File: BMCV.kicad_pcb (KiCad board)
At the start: 4 copper layers, 80 x 108 mm, 363 parts, among them J1 AudioJack2_SwitchT, J10 AudioJack2_SwitchT, J11 AudioJack2_SwitchT, J12 AudioJack2_SwitchT, J13 DebugPins, J14 USB_C_Receptacle_USB2.0_14P, J16 Conn_02x08_Eurorack, J2 AudioJack2_SwitchT, J3 AudioJack2_SwitchT, J4 AudioJack2_SwitchT, J5 AudioJack2_SwitchT, J6 AudioJack2_SwitchT, J7 AudioJack2_SwitchT, J8 AudioJack2_SwitchT, J9 AudioJack2_SwitchT, SW1 TC002-N11AS2XT-RGB, SW10 TC002-N11AS2XT-RGB, SW11 TC002-N11AS2XT-RGB, SW12 TC002-N11AS2XT-RGB, SW13 TC002-N11AS2XT-RGB, SW14 Reset, SW15 Boot, SW2 TC002-N11AS2XT-RGB, SW3 TC002-N11AS2XT-RGB, SW4 TC002-N11AS2XT-RGB, SW5 TC002-N11AS2XT-RGB, SW6 TC002-N11AS2XT-RGB, SW7 TC002-N11AS2XT-RGB, SW8 TC002-N11AS2XT-RGB, SW9 TC002-N11AS2XT-RGB, U1 PEL12T-4225S-S1024, U10 WS2811F, U11 WS2811F, U12 WS2811F, U13 WS2811F, U14 WS2811F, U15 WS2811F, U16 WS2811F, U17 WS2811F, U18 WS2811F, U19 WS2811F, U2 PEL12T-4225S-S1024, U20 WS2811F, U21 WS2811F, U22 WS2811F, U23 WS2811F, U24 WS2811F, U25 WS2811F, U26 WS2811F, U27 WS2811F, U28 WS2811F, U29 WS2811F, U3 PEL12T-4225S-S1024, U30 MCP23S17_SS, U31 MCP23S17_SS, U32 TXS0108EPW, U33 AD7367-5, U34 AD5754R, U35 AD5754R, U36 STM32G474CETx, U37 MB85RS64PNF-G-JNERE1, U38 OPA4171, U39 OPA4171, U4 PEL12T-4225S-S1024, U40 OPA4171, U41 TLV76733, U5 PEL12T-4225S-S1024, U6 PEL12T-4225S-S1024, U7 PEL12T-4225S-S1024, U8 PEL12T-4225S-S1024, U9 WS2811F, Y1 38.4MHz 10pF

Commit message: pcb
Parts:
- added C112: 100n, Capacitor_SMD:C_0402_1005Metric, B.Cu at (77.8, 93.0)
- added U42: 74AHCT1G125, Package_TO_SOT_SMD:SOT-353_SC-70-5, B.Cu at (78.5, 95.3)
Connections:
- U32 pad 1: WSDATA -> unconnected-(U32-A1-Pad1)
- U32 pad 20: WSDATA_5V -> unconnected-(U32-B1-Pad20)
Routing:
- net WSDATA_5V: track 9.00 -> 6.08 mm
- net +5V: track 642.4 -> 644.6 mm
- net GND: track 222.1 -> 224.2 mm, vias 638 -> 635
- net WSDATA: track 8.32 -> 9.58 mm, vias 0 -> 2

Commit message: stuff
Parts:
- moved C9 0.11 mm to (80.8, 100.7)
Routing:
- net +5V: track 644.6 -> 647.5 mm
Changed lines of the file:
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@@
 			(at 0 -4.85 0)
 			(layer "B.Fab")
+			(hide yes)
 			(effects
 				(font
@@
 			(at 0 -4.85 0)
 			(layer "B.Fab")
+			(hide yes)
 			(effects
 				(font
@@
 			)
 		)
-		(property "LCSC Part #" "C392906"
+		(property "LCSC Part #" "C392905"
 			(at 0 0 180)
 			(unlocked yes)
@@
 	(footprint "Capacitor_SMD:C_0603_1608Metric"
 		(layer "B.Cu")
-		(at 80.65 100.6 135)
+		(at 80.75 100.65 135)
 		(descr "Capacitor SMD 0603 (1608 Metric), square (rectangular) end terminal, IPC_7351 nominal, (Body size source: IPC-SM-782 page 76, https://www.pcb-3d.com/wordpress/wp-content/uploads/ipc-sm-782a_amendment_1_and_2.pdf), generated with kicad-footprint-generator")
 		(tags "capacitor")
@@
 			(at 0 -4.85 0)
 			(layer "B.Fab")
+			(hide yes)
 			(effects
 				(font
@@
 			)
 		)
-		(property "LCSC Part #" "C392906"
+		(property "LCSC Part #" "C392905"
 			(at 0 0 180)
 			(unlocked yes)
@@
 	)
 	(segment
+		(start 83.212564 100.291386)
+		(end 82.220175 100.291386)
+		(width 0.3)
+		(layer "B.Cu")
+		(net 39)
+	)
+	(segment
 		(start 84.021178 101.1)
 		(end 83.610589 100.689411)
@@
 	)
 	(segment
+		(start 83.610589 100.689411)
+		(end 83.212564 100.291386)
+		(width 0.3)
+		(layer "B.Cu")
+		(net 39)
+	)
+	(segment
 		(start 84.5 101.93934)
 		(end 84.5 101.232234)
@@
 	)
 	(segment
-		(start 82.05463 100.291386)
-		(end 81.198008 101.148008)
+		(start 82.220175 100.291386)
+		(end 81.363553 101.148008)
 		(width 0.3)
 		(layer "B.Cu")
@@
 	)
 	(segment
-		(start 83.212564 100.291386)
-		(end 82.05463 100.291386)
+		(start 81.363553 101.148008)
+		(end 81.198008 101.148008)
 		(width 0.3)
 		(layer "B.Cu")
@@
 	)
 	(segment
-		(start 83.610589 100.689411)
-		(end 83.212564 100.291386)
-		(width 0.3)
-		(layer "B.Cu")
-		(net 39)
-	)
-	(segment
 		(start 97.4 96.9)
 		(end 97.4 98.3)
@@
 	)
 	(via
-		(at 75 95)
+		(at 75.05 93.15)
 		(size 0.6)
 		(drill 0.25)
@@
 	)
 	(via
-		(at 79.45 100.7)
+		(at 79.603984 100.7)
 		(size 0.6)
 		(drill 0.25)
@@
 	)
 	(segment
-		(start 79.453984 100.7)
-		(end 80.101992 100.051992)
-		(width 0.3)
-		(layer "B.Cu")
-		(net 53)
-	)
-	(segment
 		(start 45.8 134.55)
 		(end 45.2 133.95)
@@
 	)
 	(segment
+		(start 79.603984 100.7)
+		(end 80.201992 100.101992)
+		(width 0.3)
+		(layer "B.Cu")
+		(net 53)
+	)
+	(segment
 		(start 106.345 48.945)
 		(end 106.345 49.495)
@@
 	)
 	(segment
-		(start 79.45 100.7)
-		(end 79.453984 100.7)
-		(width 0.3)
-		(layer "B.Cu")
-		(net 53)
-	)
-	(segment
 		(start 57 127.79)
 		(end 56.33 127.79)
@@
 	)
 	(segment
+		(start 80.125 93.675)
+		(end 80.175 93.675)
+		(width 0.3)
+		(layer "B.Cu")
+		(net 54)
+	)
+	(segment
 		(start 76.9 78.23)
 		(end 76.13 79)
@@
 	)
 	(segment
+		(start 77.471178 93.35)
+		(end 79.8 93.35)
+		(width 0.3)
+		(layer "B.Cu")
+		(net 54)
+	)
+	(segment
 		(start 85.3 72.61)
 		(end 83.8 72.61)
@@
 	)
 	(segment
+		(start 80.15 93.35)
+		(end 80.5 93)
+		(width 0.3)
+		(layer "B.Cu")
+		(net 54)
+	)
+	(segment
 		(start 76.53 79.4)
 		(end 76.13 79)
@@
 	)
 	(segment
+		(start 80.175 93.675)
+		(end 80.5 93.35)
+		(width 0.5)
+		(layer "B.Cu")
+		(net 54)
+	)
+	(segment
 		(start 97.2 88.6)
 		(end 97.2 90)
@@
 	)
 	(segment
+		(start 79.8 93.35)
+		(end 80.15 93.35)
+		(width 0.3)
+		(layer "B.Cu")
+		(net 54)
+	)
+	(segment
 		(start 36.51 81.39)
 		(end 36.8 81.39)
@@
 	)
 	(segment
-		(start 78.975 94.840761)
-		(end 78.327868 94.193629)
-		(width 0.3)
-		(layer "B.Cu")
-		(net 54)
-	)
-	(segment
 		(start 45.7 61)
 		(end 41.5 61)
@@
 	)
 	(segment
+		(start 79.8 93.35)
+		(end 80.125 93.675)
+		(width 0.3)
+		(layer "B.Cu")
+		(net 54)
+	)
+	(segment
 		(start 76.53 86.663984)
 		(end 75.951992 87.241992)
@@
 	(segment
 		(start 78.975 94.875)
-		(end 80.5 93.35)
+		(end 80.175 93.675)
 		(width 0.5)
 		(layer "B.Cu")
@@
 	)
 	(segment
+		(start 77.410589 93.289411)
+		(end 77.471178 93.35)
+		(width 0.3)
+		(layer "B.Cu")
+		(net 54)
+	)
+	(segment
 		(start 64.08 58.129999)
 		(end 63.749999 58.46)
@@
 	)
 	(segment
-		(start 99.45 100)
-		(end 98.15 101.3)
+		(start 98.15 101.3)
+		(end 93.967766 101.3)
 		(width 0.2)
 		(layer "B.Cu")
@@
 	)
 	(segment
-		(start 93.967766 101.3)
-		(end 91.327215 103.940551)
+		(start 99.45 98.5)
+		(end 99.45 100)
 		(width 0.2)
 		(layer "B.Cu")
@@
 	)
 	(segment
-		(start 98.15 101.3)
-		(end 93.967766 101.3)
+		(start 99.45 100)
+		(end 98.15 101.3)
 		(width 0.2)
 		(layer "B.Cu")
@@
 	)
 	(segment
-		(start 99.45 98.5)
-		(end 99.45 100)
+		(start 93.967766 101.3)
+		(end 91.327215 103.940551)
+		(width 0.2)
+		(layer "B.Cu")
+		(net 83)
+	)
+	(segment
+		(start 99.25 98.3)
+		(end 99.45 98.5)
 		(width 0.2)
 		(layer "B.Cu")
@@
 	)
 	(segment
-		(start 99.95 100.222182)
-		(end 99.95 98.5)
+		(start 99.95 98.5)
+		(end 100.15 98.3)
 		(width 0.2)
 		(layer "B.Cu")
@@
 		(width 0.2)
 		(layer "B.Cu")
+		(net 84)
+	)
+	(segment
+		(start 99.95 100.222182)
+		(end 99.95 98.5)
+		(width 0.2)
+		(layer "B.Cu")

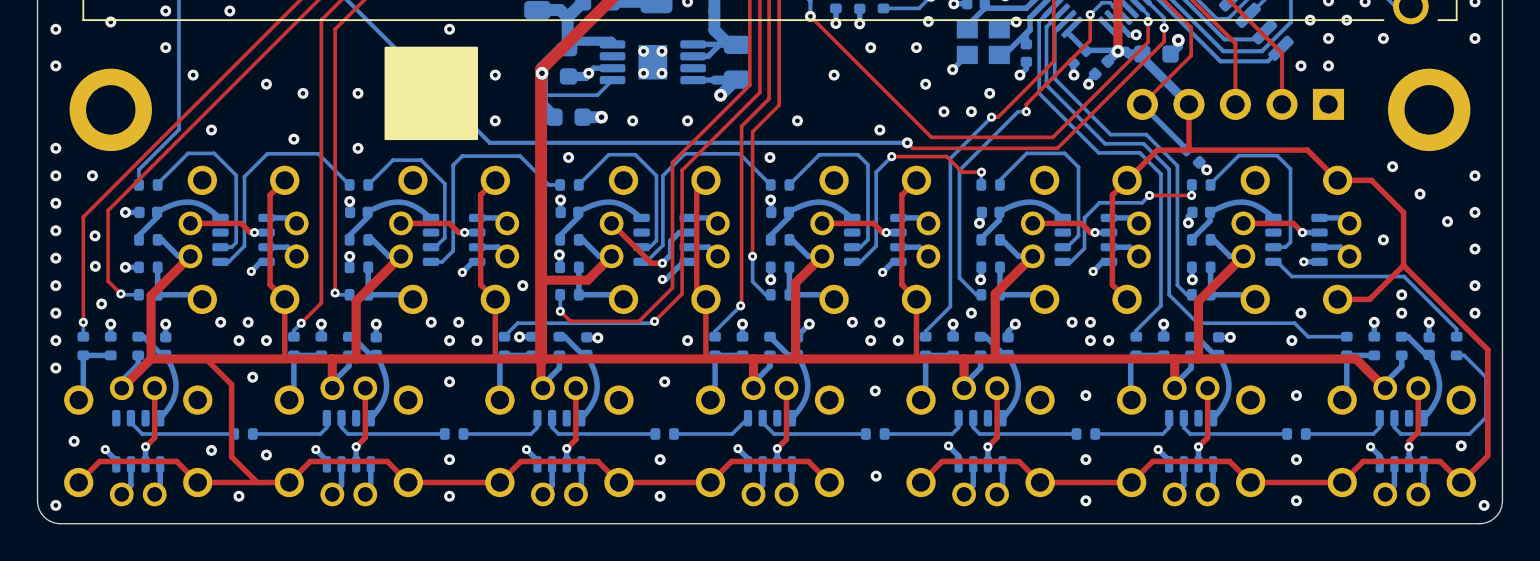
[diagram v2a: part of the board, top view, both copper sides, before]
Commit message: update footprint slightly to possibly support 228C series LED Switches
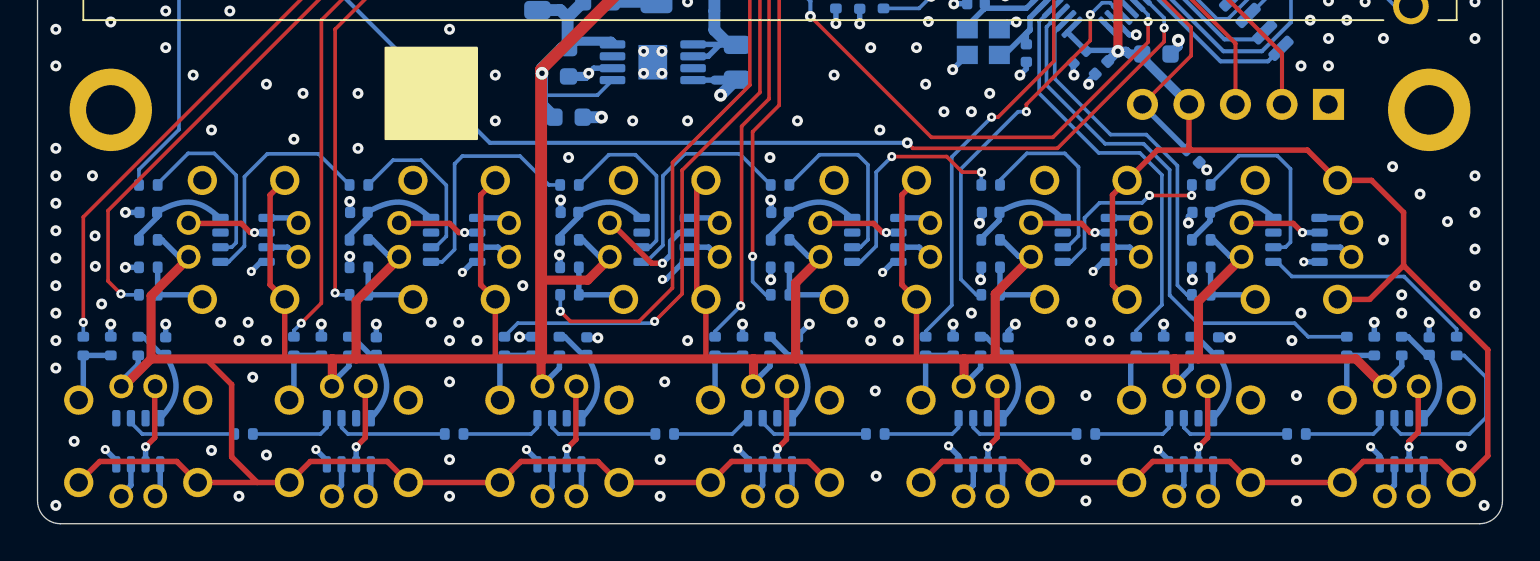
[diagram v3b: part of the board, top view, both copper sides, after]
